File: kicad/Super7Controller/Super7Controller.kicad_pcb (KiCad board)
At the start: 2 copper layers, 106.7 x 25.4 mm, 20 parts, among them P3 CONN_01X13, P4 CONN_01X09, U1 ULN2003A, U2 HiLetgo_ESP-WROOM-32_Developm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

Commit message: add anchor
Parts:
- added REF**: Socket_Strip_Straight_1x04, misc:Strip_1x04, F.Cu at (168.3, 68.6)
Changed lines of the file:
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@@
+    )
+  )
+  (module misc:Strip_1x04 (layer F.Cu)
+    (at 168.275 68.58 90)
+    (descr "Through hole socket strip")
+    (tags "socket strip")
+    (fp_text reference REF** (at 0 -5.1 90) (layer F.SilkS) hide
+      (effects (font (size 1 1) (thickness 0.15)))
+    )
+    (fp_text value Socket_Strip_Straight_1x04 (at 0 -3.1 90) (layer F.Fab) hide
+      (effects (font (size 1 1) (thickness 0.15)))
+    )
+    (fp_line (start -1.75 -1.75) (end -1.75 1.75) (layer F.CrtYd) (width 0.05))
+    (fp_line (start 9.4 -1.75) (end 9.4 1.75) (layer F.CrtYd) (width 0.05))
+    (fp_line (start -1.75 -1.75) (end 9.4 -1.75) (layer F.CrtYd) (width 0.05))
+    (fp_line (start -1.75 1.75) (end 9.4 1.75) (layer F.CrtYd) (width 0.05))
+    (pad 1 thru_hole oval (at 0 0 90) (size 1.7272 2.032) (drill 1.016) (layers *.Cu *.Mask))
+    (pad 2 thru_hole oval (at 2.54 0 90) (size 1.7272 2.032) (drill 1.016) (layers *.Cu *.Mask))
+    (pad 3 thru_hole oval (at 5.08 0 90) (size 1.7272 2.032) (drill 1.016) (layers *.Cu *.Mask))
+    (pad 4 thru_hole oval (at 7.62 0 90) (size 1.7272 2.032) (drill 1.016) (layers *.Cu *.Mask))
+    (model Socket_Strips.3dshapes/Socket_Strip_Straight_1x04.wrl
+      (at (xyz 0.15 0 0))
+      (scale (xyz 1 1 1))
+      (rotate (xyz 0 0 180))
     )
   )

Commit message: imported routes into kicad
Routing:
- net Net-(R14-Pad1): track 0.00 -> 105.2 mm
- net Net-(R9-Pad1): track 0.00 -> 103.1 mm
- net Net-(R7-Pad1): track 0.00 -> 97.7 mm
- net Net-(R12-Pad1): track 0.00 -> 90.4 mm, vias 0 -> 1
- net Net-(R13-Pad1): track 0.00 -> 89.9 mm, vias 0 -> 1
- net Net-(R5-Pad1): track 0.00 -> 80.4 mm
- net Net-(R15-Pad1): track 0.00 -> 80.3 mm
- net Net-(R16-Pad1): track 0.00 -> 79.8 mm
- net Net-(R3-Pad1): track 0.00 -> 71.4 mm
- net Net-(R2-Pad1): track 0.00 -> 62.7 mm
- net Net-(R8-Pad1): track 0.00 -> 60.8 mm
- net Net-(R1-Pad1): track 0.00 -> 58.2 mm, vias 0 -> 1
- net Net-(R10-Pad1): track 0.00 -> 57.8 mm, vias 0 -> 1
- net Net-(R11-Pad1): track 0.00 -> 57.8 mm, vias 0 -> 1
- net Net-(R4-Pad1): track 0.00 -> 57.5 mm
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
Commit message: delete tracks
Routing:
- net Net-(R14-Pad1): track 105.2 -> 0.00 mm
- net Net-(R9-Pad1): track 103.1 -> 0.00 mm
- net Net-(R7-Pad1): track 97.7 -> 0.00 mm
- net Net-(R12-Pad1): track 90.4 -> 0.00 mm, vias 1 -> 0
- net Net-(R13-Pad1): track 89.9 -> 0.00 mm, vias 1 -> 0
- net Net-(R5-Pad1): track 80.4 -> 0.00 mm
- net Net-(R15-Pad1): track 80.3 -> 0.00 mm
- net Net-(R16-Pad1): track 79.8 -> 0.00 mm
- net Net-(R3-Pad1): track 71.4 -> 0.00 mm
- net Net-(R2-Pad1): track 62.7 -> 0.00 mm
- net Net-(R8-Pad1): track 60.8 -> 0.00 mm
- net Net-(R1-Pad1): track 58.2 -> 0.00 mm, vias 1 -> 0
- net Net-(R10-Pad1): track 57.8 -> 0.00 mm, vias 1 -> 0
- net Net-(R11-Pad1): track 57.8 -> 0.00 mm, vias 1 -> 0
- net Net-(R4-Pad1): track 57.5 -> 0.00 mm
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
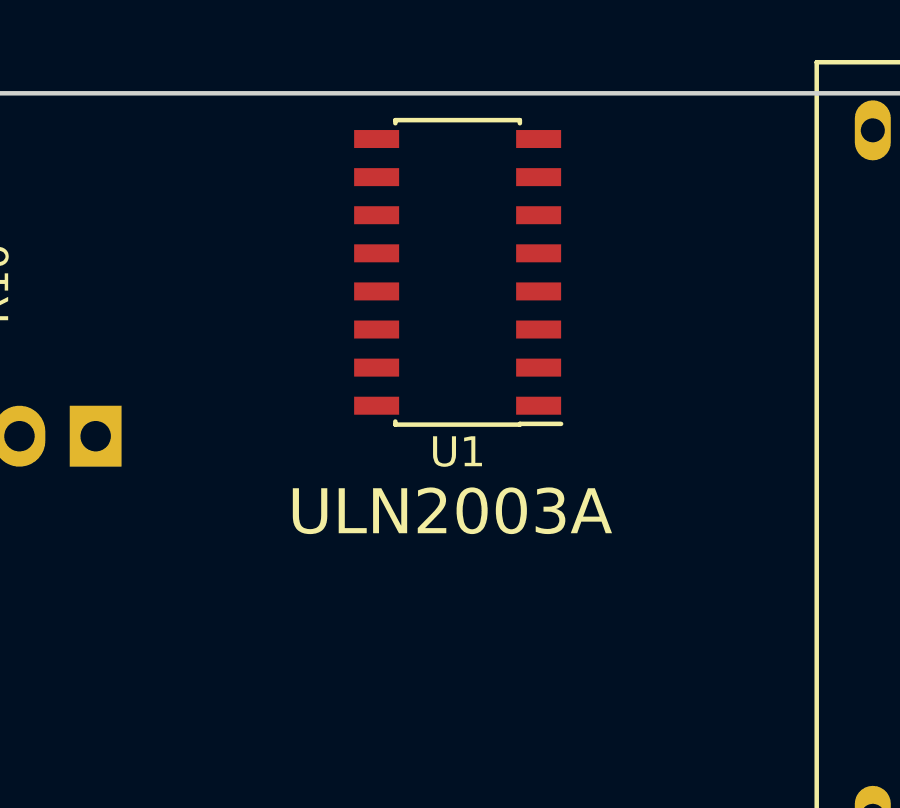
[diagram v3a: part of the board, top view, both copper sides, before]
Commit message: move ULN to the back
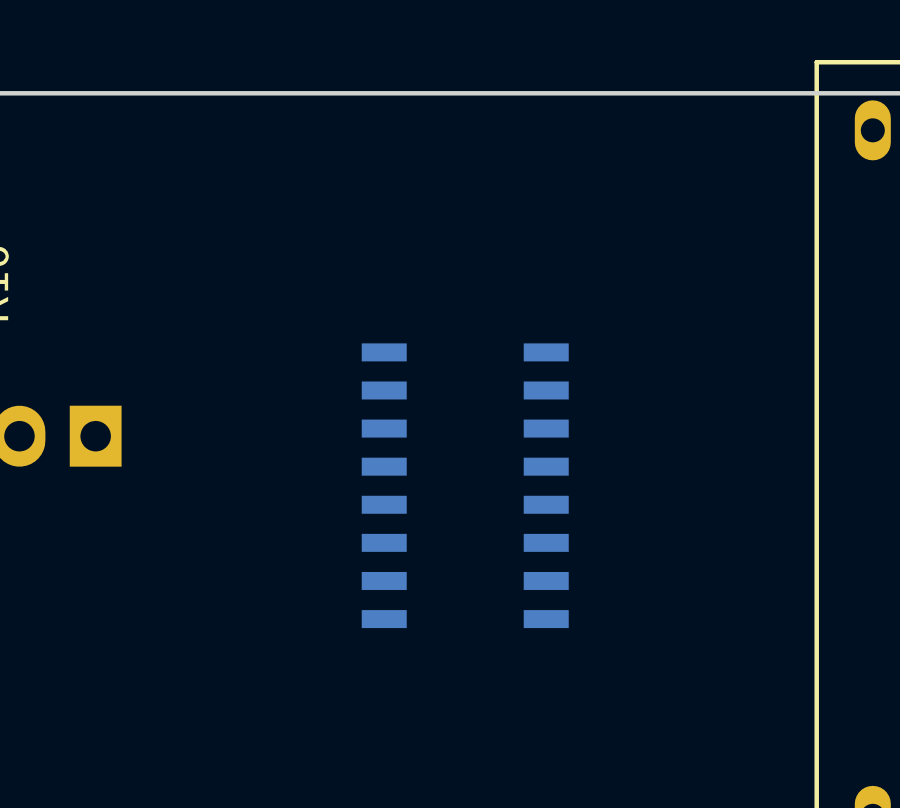
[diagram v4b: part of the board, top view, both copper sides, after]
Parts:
- U1: moved to B.Cu
- moved U1 7.12 mm to (114.6, 66.4)
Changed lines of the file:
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@@
     )
   )
-  (module Housings_SOIC:SOIC-16_3.9x9.9mm_Pitch1.27mm (layer F.Cu)
-    (at 114.3 59.309 180)
+  (module Housings_SOIC:SOIC-16_3.9x9.9mm_Pitch1.27mm (layer B.Cu)
+    (at 114.554 66.421 180)
     (descr "16-Lead Plastic Small Outline (SL) - Narrow, 3.90 mm Body [SOIC] (see Microchip Packaging Specification 00000049BS.pdf)")
     (tags "SOIC 1.27")
     (attr smd)
-    (fp_text reference U1 (at 0 -6 180) (layer F.SilkS)
-      (effects (font (size 1 1) (thickness 0.15)))
+    (fp_text reference U1 (at 0 6 180) (layer B.SilkS)
+      (effects (font (size 1 1) (thickness 0.15)) (justify mirror))
     )
-    (fp_text value ULN2003A (at 0 6 180) (layer F.Fab)
-      (effects (font (size 1 1) (thickness 0.15)))
+    (fp_text value ULN2003A (at 0 -6 180) (layer B.Fab)
+      (effects (font (size 1 1) (thickness 0.15)) (justify mirror))
     )
-    (fp_text user %R (at 0 0 180) (layer F.Fab)
-      (effects (font (size 0.9 0.9) (thickness 0.135)))
+    (fp_text user %R (at 0 0 180) (layer B.Fab)
+      (effects (font (size 0.9 0.9) (thickness 0.135)) (justify mirror))
     )
-    (fp_line (start -0.95 -4.95) (end 1.95 -4.95) (layer F.Fab) (width 0.15))
-    (fp_line (start 1.95 -4.95) (end 1.95 4.95) (layer F.Fab) (width 0.15))
-    (fp_line (start 1.95 4.95) (end -1.95 4.95) (layer F.Fab) (width 0.15))
-    (fp_line (start -1.95 4.95) (end -1.95 -3.95) (layer F.Fab) (width 0.15))
-    (fp_line (start -1.95 -3.95) (end -0.95 -4.95) (layer F.Fab) (width 0.15))
-    (fp_line (start -3.7 -5.25) (end -3.7 5.25) (layer F.CrtYd) (width 0.05))
-    (fp_line (start 3.7 -5.25) (end 3.7 5.25) (layer F.CrtYd) (width 0.05))
-    (fp_line (start -3.7 -5.25) (end 3.7 -5.25) (layer F.CrtYd) (width 0.05))
-    (fp_line (start -3.7 5.25) (end 3.7 5.25) (layer F.CrtYd) (width 0.05))
-    (fp_line (start -2.075 -5.075) (end -2.075 -5.05) (layer F.SilkS) (width 0.15))
-    (fp_line (start 2.075 -5.075) (end 2.075 -4.97) (layer F.SilkS) (width 0.15))
-    (fp_line (start 2.075 5.075) (end 2.075 4.97) (layer F.SilkS) (width 0.15))
-    (fp_line (start -2.075 5.075) (end -2.075 4.97) (layer F.SilkS) (width 0.15))
-    (fp_line (start -2.075 -5.075) (end 2.075 -5.075) (layer F.SilkS) (width 0.15))
-    (fp_line (start -2.075 5.075) (end 2.075 5.075) (layer F.SilkS) (width 0.15))
-    (fp_line (start -2.075 -5.05) (end -3.45 -5.05) (layer F.SilkS) (width 0.15))
-    (pad 1 smd rect (at -2.7 -4.445 180) (size 1.5 0.6) (layers F.Cu F.Paste F.Mask)
+    (fp_line (start -0.95 4.95) (end 1.95 4.95) (layer B.Fab) (width 0.15))
+    (fp_line (start 1.95 4.95) (end 1.95 -4.95) (layer B.Fab) (width 0.15))
+    (fp_line (start 1.95 -4.95) (end -1.95 -4.95) (layer B.Fab) (width 0.15))
+    (fp_line (start -1.95 -4.95) (end -1.95 3.95) (layer B.Fab) (width 0.15))
+    (fp_line (start -1.95 3.95) (end -0.95 4.95) (layer B.Fab) (width 0.15))
+    (fp_line (start -3.7 5.25) (end -3.7 -5.25) (layer B.CrtYd) (width 0.05))
+    (fp_line (start 3.7 5.25) (end 3.7 -5.25) (layer B.CrtYd) (width 0.05))
+    (fp_line (start -3.7 5.25) (end 3.7 5.25) (layer B.CrtYd) (width 0.05))
+    (fp_line (start -3.7 -5.25) (end 3.7 -5.25) (layer B.CrtYd) (width 0.05))
+    (fp_line (start -2.075 5.075) (end -2.075 5.05) (layer B.SilkS) (width 0.15))
+    (fp_line (start 2.075 5.075) (end 2.075 4.97) (layer B.SilkS) (width 0.15))
+    (fp_line (start 2.075 -5.075) (end 2.075 -4.97) (layer B.SilkS) (width 0.15))
+    (fp_line (start -2.075 -5.075) (end -2.075 -4.97) (layer B.SilkS) (width 0.15))
+    (fp_line (start -2.075 5.075) (end 2.075 5.075) (layer B.SilkS) (width 0.15))
+    (fp_line (start -2.075 -5.075) (end 2.075 -5.075) (layer B.SilkS) (width 0.15))
+    (fp_line (start -2.075 5.05) (end -3.45 5.05) (layer B.SilkS) (width 0.15))
+    (pad 1 smd rect (at -2.7 4.445 180) (size 1.5 0.6) (layers B.Cu B.Paste B.Mask)
       (net 43 "Net-(U1-Pad1)"))
-    (pad 2 smd rect (at -2.7 -3.175 180) (size 1.5 0.6) (layers F.Cu F.Paste F.Mask)
+    (pad 2 smd rect (at -2.7 3.175 180) (size 1.5 0.6) (layers B.Cu B.Paste B.Mask)
       (net 44 "Net-(U1-Pad2)"))
-    (pad 3 smd rect (at -2.7 -1.905 180) (size 1.5 0.6) (layers F.Cu F.Paste F.Mask)
+    (pad 3 smd rect (at -2.7 1.905 180) (size 1.5 0.6) (layers B.Cu B.Paste B.Mask)
       (net 45 "Net-(U1-Pad3)"))
-    (pad 4 smd rect (at -2.7 -0.635 180) (size 1.5 0.6) (layers F.Cu F.Paste F.Mask)
+    (pad 4 smd rect (at -2.7 0.635 180) (size 1.5 0.6) (layers B.Cu B.Paste B.Mask)
       (net 46 "Net-(U1-Pad4)"))
-    (pad 5 smd rect (at -2.7 0.635 180) (size 1.5 0.6) (layers F.Cu F.Paste F.Mask)
+    (pad 5 smd rect (at -2.7 -0.635 180) (size 1.5 0.6) (layers B.Cu B.Paste B.Mask)
       (net 47 "Net-(U1-Pad5)"))
-    (pad 6 smd rect (at -2.7 1.905 180) (size 1.5 0.6) (layers F.Cu F.Paste F.Mask)
+    (pad 6 smd rect (at -2.7 -1.905 180) (size 1.5 0.6) (layers B.Cu B.Paste B.Mask)
       (net 48 "Net-(U1-Pad6)"))
-    (pad 7 smd rect (at -2.7 3.175 180) (size 1.5 0.6) (layers F.Cu F.Paste F.Mask)
+    (pad 7 smd rect (at -2.7 -3.175 180) (size 1.5 0.6) (layers B.Cu B.Paste B.Mask)
       (net 49 "Net-(U1-Pad7)"))
-    (pad 8 smd rect (at -2.7 4.445 180) (size 1.5 0.6) (layers F.Cu F.Paste F.Mask)
+    (pad 8 smd rect (at -2.7 -4.445 180) (size 1.5 0.6) (layers B.Cu B.Paste B.Mask)
       (net 1 GND))
-    (pad 9 smd rect (at 2.7 4.445 180) (size 1.5 0.6) (layers F.Cu F.Paste F.Mask)
+    (pad 9 smd rect (at 2.7 -4.445 180) (size 1.5 0.6) (layers B.Cu B.Paste B.Mask)
       (net 25 "Net-(U1-Pad9)"))
-    (pad 10 smd rect (at 2.7 3.175 180) (size 1.5 0.6) (layers F.Cu F.Paste F.Mask)
+    (pad 10 smd rect (at 2.7 -3.175 180) (size 1.5 0.6) (layers B.Cu B.Paste B.Mask)
       (net 26 "Net-(U1-Pad10)"))
-    (pad 11 smd rect (at 2.7 1.905 180) (size 1.5 0.6) (layers F.Cu F.Paste F.Mask)
+    (pad 11 smd rect (at 2.7 -1.905 180) (size 1.5 0.6) (layers B.Cu B.Paste B.Mask)
       (net 15 DC_6))
-    (pad 12 smd rect (at 2.7 0.635 180) (size 1.5 0.6) (layers F.Cu F.Paste F.Mask)
+    (pad 12 smd rect (at 2.7 -0.635 180) (size 1.5 0.6) (layers B.Cu B.Paste B.Mask)
       (net 14 DC_5))
-    (pad 13 smd rect (at 2.7 -0.635 180) (size 1.5 0.6) (layers F.Cu F.Paste F.Mask)
+    (pad 13 smd rect (at 2.7 0.635 180) (size 1.5 0.6) (layers B.Cu B.Paste B.Mask)
       (net 10 DC_4))
-    (pad 14 smd rect (at 2.7 -1.905 180) (size 1.5 0.6) (layers F.Cu F.Paste F.Mask)
+    (pad 14 smd rect (at 2.7 1.905 180) (size 1.5 0.6) (layers B.Cu B.Paste B.Mask)
       (net 5 DC_3))
-    (pad 15 smd rect (at 2.7 -3.175 180) (size 1.5 0.6) (layers F.Cu F.Paste F.Mask)
+    (pad 15 smd rect (at 2.7 3.175 180) (size 1.5 0.6) (layers B.Cu B.Paste B.Mask)
       (net 4 DC_2))
-    (pad 16 smd rect (at 2.7 -4.445 180) (size 1.5 0.6) (layers F.Cu F.Paste F.Mask)
+    (pad 16 smd rect (at 2.7 4.445 180) (size 1.5 0.6) (layers B.Cu B.Paste B.Mask)
       (net 3 DC_1))
     (model ${KISYS3DMOD}/Housings_SOIC.3dshapes/SOIC-16_3.9x9.9mm_Pitch1.27mm.wrl
@@
   (gr_line (start 175.895 71.12) (end 175.895 76.2) (angle 90) (layer Edge.Cuts) (width 0.15))
   (gr_line (start 175.895 55.88) (end 175.895 60.96) (angle 90) (layer Edge.Cuts) (width 0.15))
-  (gr_text ULN2003A (at 114.046 67.31) (layer F.SilkS)
-    (effects (font (size 1.5 1.5) (thickness 0.3)))
+  (gr_text ULN2003A (at 114.427 74.168) (layer B.SilkS)
+    (effects (font (size 1.5 1.5) (thickness 0.3)) (justify mirror))
   )
   (gr_text "Anchor This Side" (at 166.37 64.135 90) (layer B.SilkS)

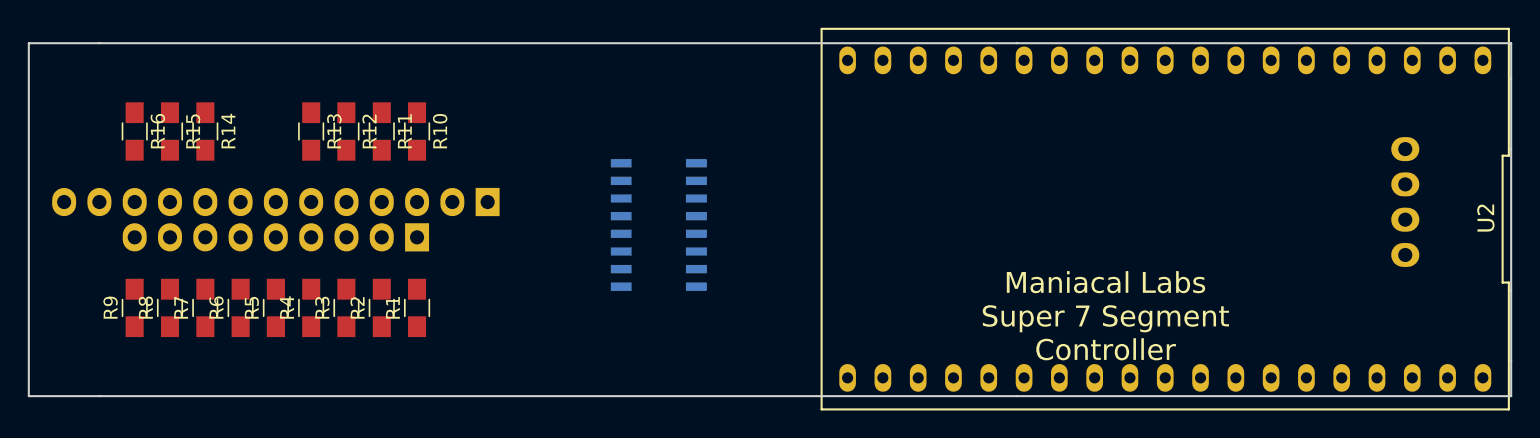
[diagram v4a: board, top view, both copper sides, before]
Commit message: import routed design into KiCad
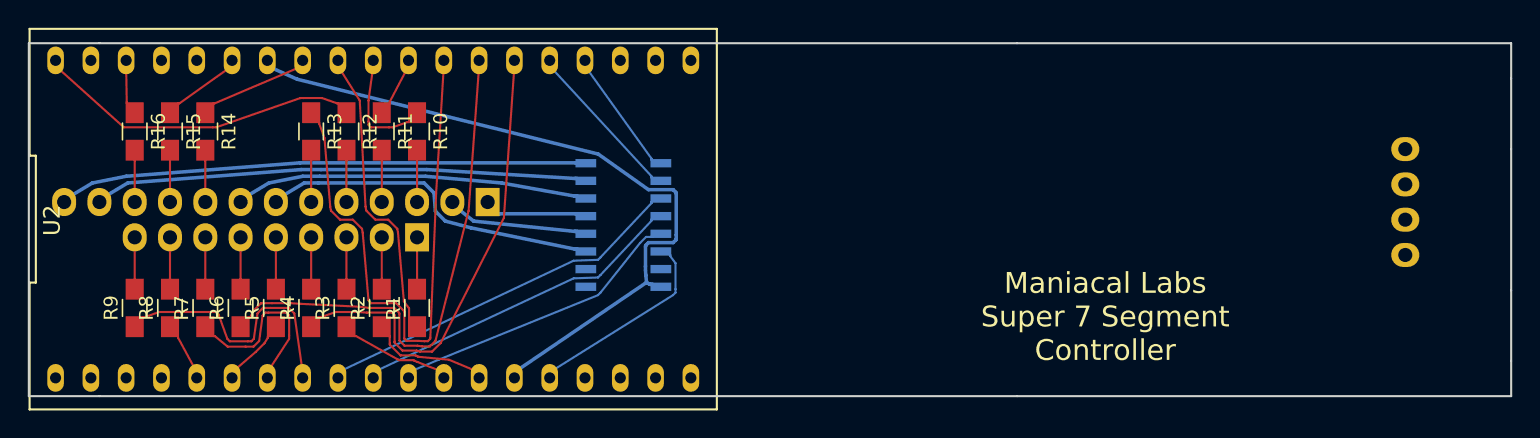
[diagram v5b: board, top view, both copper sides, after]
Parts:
- moved U2 57.0 mm to (94.0, 66.0), turned to 0 degrees
- moved U1 2.55 mm to (112.0, 66.4)
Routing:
- net GND: track 0.00 -> 53.0 mm
- net Net-(R13-Pad1): track 0.00 -> 42.2 mm
- net DC_6: track 0.00 -> 38.1 mm
- net Net-(R6-Pad1): track 0.00 -> 37.8 mm
- net DC_5: track 0.00 -> 35.6 mm
- net Net-(R4-Pad1): track 0.00 -> 33.7 mm
- net Net-(U1-Pad6): track 0.00 -> 27.4 mm
- net DC_4: track 0.00 -> 25.5 mm
- net DC_3: track 0.00 -> 24.8 mm
- net Net-(U1-Pad5): track 0.00 -> 24.5 mm
- net Net-(R12-Pad1): track 0.00 -> 23.8 mm
- net Net-(U1-Pad4): track 0.00 -> 21.7 mm
- net Net-(R1-Pad1): track 0.00 -> 21.5 mm
- net Net-(R9-Pad1): track 0.00 -> 19.9 mm
- net Net-(U1-Pad3): track 0.00 -> 14.7 mm
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
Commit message: adjust edge cuts and remove unneeded parts
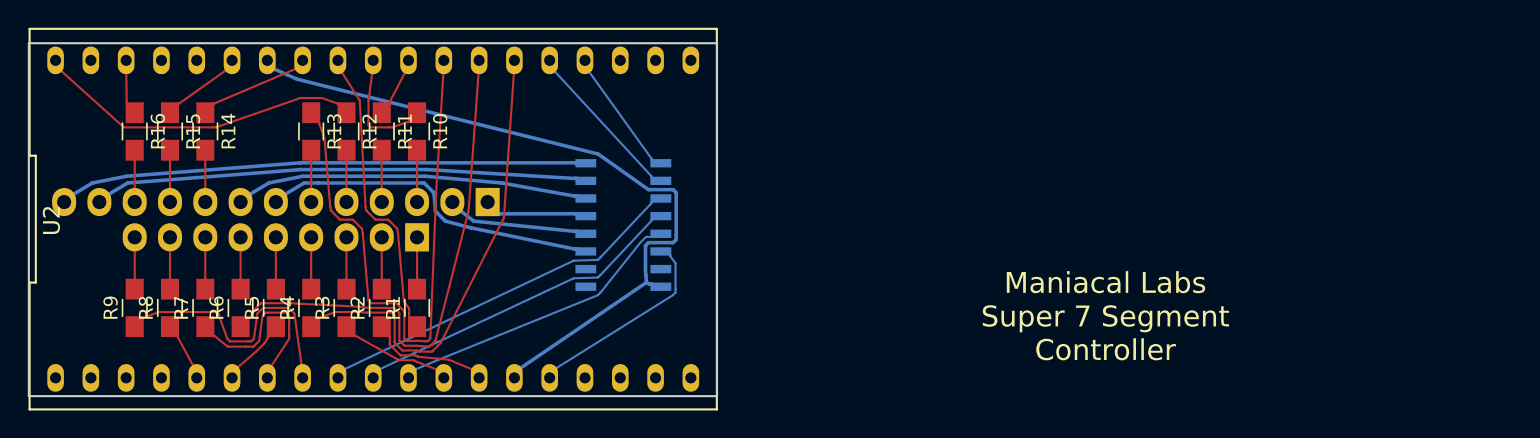
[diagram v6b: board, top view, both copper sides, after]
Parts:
- removed REF**: Socket_Strip_Straight_1x04, misc:Strip_1x04
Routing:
- net Net-(R13-Pad1): track 42.2 -> 3.98 mm
- net DC_1: track 7.47 -> 42.3 mm
- net DC_6: track 38.1 -> 3.35 mm
- net Net-(R15-Pad1): track 6.04 -> 36.5 mm
- net Net-(R16-Pad1): track 3.98 -> 32.3 mm
- net Net-(R6-Pad1): track 37.8 -> 10.9 mm
- net DC_5: track 35.6 -> 15.9 mm
- net DC_2: track 10.2 -> 29.9 mm
- net DC_4: track 25.5 -> 7.00 mm
- net DC_3: track 24.8 -> 43.3 mm
- net Net-(R4-Pad1): track 33.7 -> 43.6 mm
- net Net-(R8-Pad1): track 4.24 -> 12.2 mm
- net Net-(U1-Pad6): track 27.4 -> 21.7 mm
- net Net-(U1-Pad4): track 21.7 -> 27.0 mm
- net Net-(U1-Pad5): track 24.5 -> 19.2 mm
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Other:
- board size 106.7 x 25.4 mm -> 49.5 x 25.4 mm
- board text removed: "Anchor This Side"

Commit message: read new netlist, some errors left
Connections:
- net Net-(U1-Pad4) renamed DCD_1
- net Net-(U1-Pad5) renamed DCD_2
- net Net-(U1-Pad6) renamed DCD_3
- U1 pad 1: Net-(U1-Pad1) -> DCD_6
- U1 pad 11: DC_6 -> DC_3
- U1 pad 12: DC_5 -> DC_2
- U1 pad 13: DC_4 -> DC_1
- U1 pad 14: DC_3 -> DC_4
- U1 pad 15: DC_2 -> DC_5
- U1 pad 16: DC_1 -> DC_6
- U1 pad 2: Net-(U1-Pad2) -> DCD_5
- U1 pad 3: Net-(U1-Pad3) -> DCD_4
- U2 pad 12: Net-(U1-Pad3) -> Net-(R3-Pad1)
- U2 pad 13: Net-(U1-Pad2) -> Net-(R2-Pad1)
- U2 pad 15: Net-(U1-Pad1) -> DCD_4
- U2 pad 23: Net-(R6-Pad1) -> DCD_6
- U2 pad 24: Net-(R8-Pad1) -> DCD_5
- U2 pad 25: Net-(R16-Pad1) -> Net-(R4-Pad1)
- U2 pad 26: Net-(R15-Pad1) -> Net-(R6-Pad1)
- U2 pad 27: Net-(R4-Pad1) -> Net-(R13-Pad1)
- U2 pad 31: Net-(R2-Pad1) -> Net-(R14-Pad1)
- U2 pad 32: GND -> Net-(U2-Pad32)
- U2 pad 33: Net-(R3-Pad1) -> Net-(R15-Pad1)
- U2 pad 36: Net-(R13-Pad1) -> Net-(R16-Pad1)
- U2 pad 5: Net-(R5-Pad1) -> Net-(R8-Pad1)
- U2 pad 6: Net-(R14-Pad1) -> Net-(R5-Pad1)
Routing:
- net Net-(R13-Pad1): track 3.98 -> 42.2 mm
- net DC_1: track 42.3 -> 7.47 mm
- net DC_6: track 3.35 -> 38.1 mm
- net Net-(R15-Pad1): track 36.5 -> 6.04 mm
- net Net-(R16-Pad1): track 32.3 -> 3.98 mm
- net Net-(R6-Pad1): track 10.9 -> 37.8 mm
- net DCD_4: track 0.00 -> 22.1 mm
- net DC_5: track 15.9 -> 35.6 mm
- net DC_2: track 29.9 -> 10.2 mm
- net DC_4: track 7.00 -> 25.5 mm
- net DC_3: track 43.3 -> 24.8 mm
- net Net-(U1-Pad1): track 14.7 -> 0.00 mm
- net DCD_5: track 0.00 -> 12.0 mm
- net Net-(U1-Pad3): track 10.2 -> 0.00 mm
- net Net-(R4-Pad1): track 43.6 -> 33.7 mm
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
